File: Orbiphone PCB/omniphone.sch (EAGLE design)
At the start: 44 parts

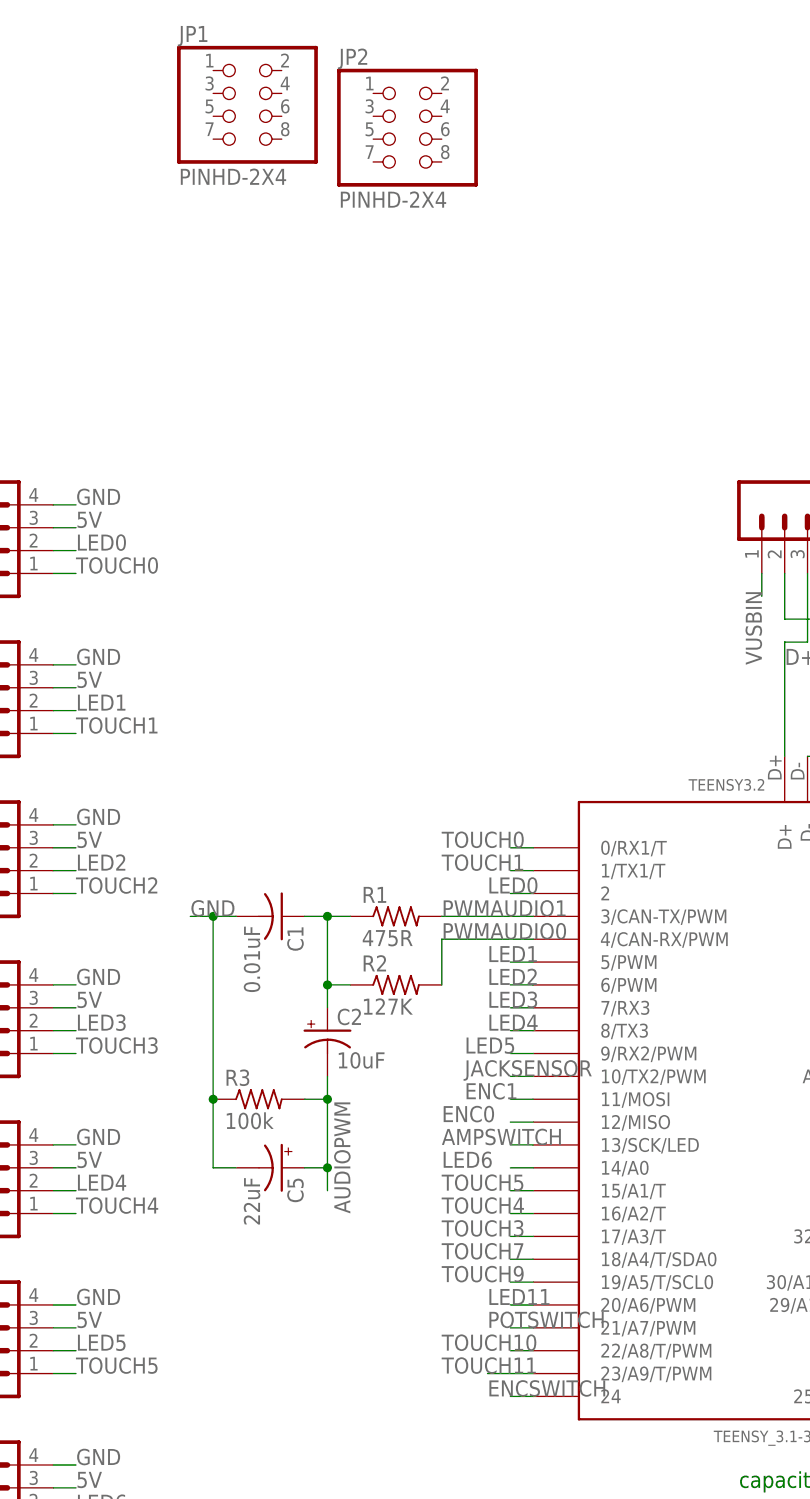
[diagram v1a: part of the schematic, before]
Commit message: changed the ampswitch as 13 doesn't work with its led on it
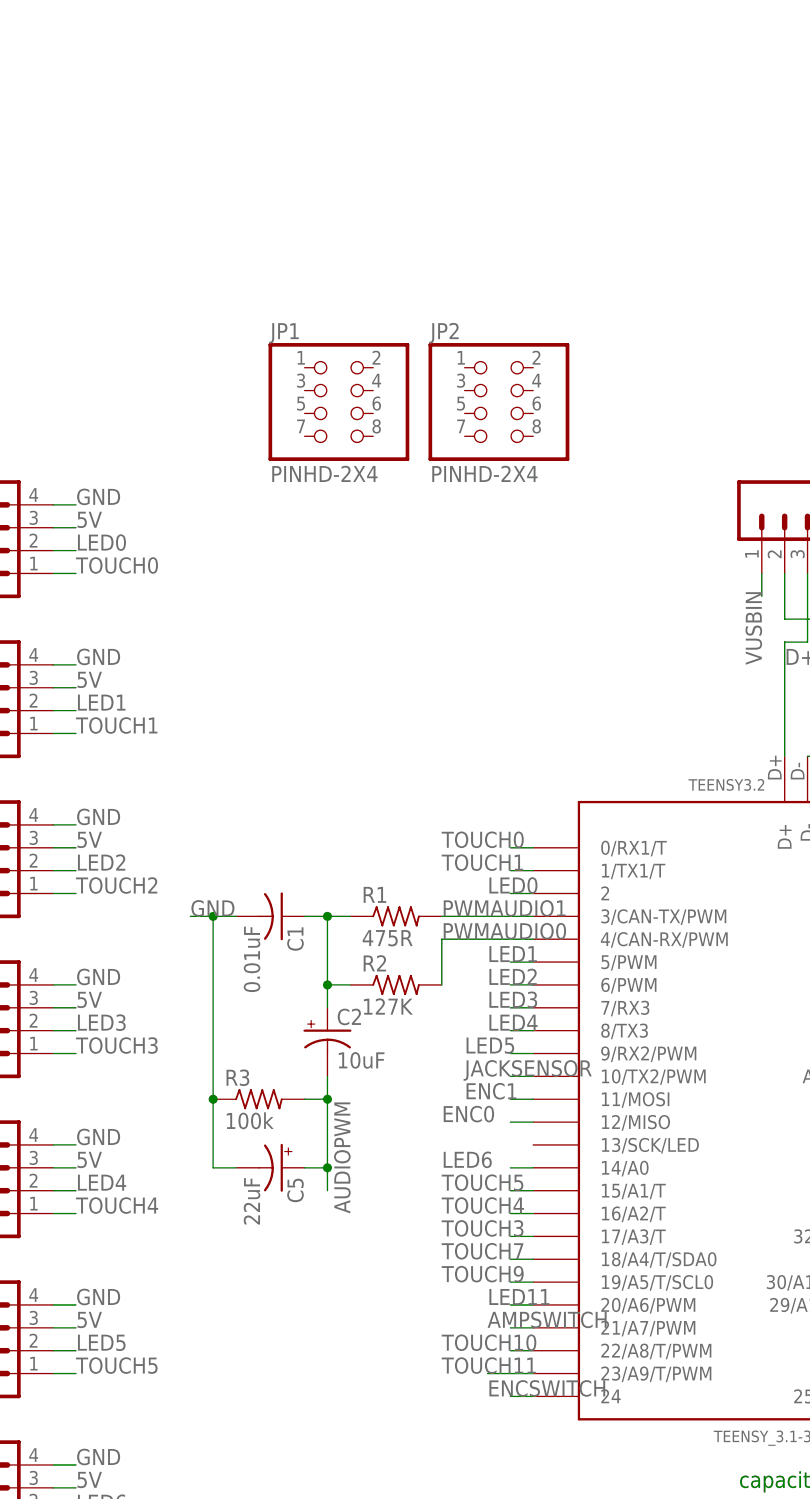
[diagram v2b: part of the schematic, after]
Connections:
- net AMPSWITCH: now also TEENSY3.2.21/A7/PWM; no longer TEENSY3.2.13/SCK/LED
- net POTSWITCH: no longer TEENSY3.2.21/A7/PWM
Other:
- moved on the sheet: JP1, JP2
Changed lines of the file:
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@@
 </instance>
 <instance part="BATTERY" gate="&gt;NAME" x="86.36" y="-5.08" smashed="yes" rot="R180"/>
-<instance part="JP1" gate="A" x="7.62" y="170.18" smashed="yes">
-<attribute name="NAME" x="1.27" y="178.435" size="1.778" layer="95"/>
-<attribute name="VALUE" x="1.27" y="162.56" size="1.778" layer="96"/>
-</instance>
-<instance part="JP2" gate="A" x="25.4" y="167.64" smashed="yes">
-<attribute name="NAME" x="19.05" y="175.895" size="1.778" layer="95"/>
-<attribute name="VALUE" x="19.05" y="160.02" size="1.778" layer="96"/>
+<instance part="JP1" gate="A" x="17.78" y="137.16" smashed="yes">
+<attribute name="NAME" x="11.43" y="145.415" size="1.778" layer="95"/>
+<attribute name="VALUE" x="11.43" y="129.54" size="1.778" layer="96"/>
+</instance>
+<instance part="JP2" gate="A" x="35.56" y="137.16" smashed="yes">
+<attribute name="NAME" x="29.21" y="145.415" size="1.778" layer="95"/>
+<attribute name="VALUE" x="29.21" y="129.54" size="1.778" layer="96"/>
 </instance>
 <instance part="R7" gate="G$1" x="91.44" y="7.62" smashed="yes">
@@
 </segment>
 <segment>
-<pinref part="TEENSY3.2" gate="G$1" pin="13/SCK/LED"/>
-<wire x1="40.64" y1="55.88" x2="38.1" y2="55.88" width="0.1524" layer="91"/>
-<label x="30.48" y="55.88" size="1.778" layer="95"/>
+<pinref part="TEENSY3.2" gate="G$1" pin="21/A7/PWM"/>
+<wire x1="40.64" y1="35.56" x2="38.1" y2="35.56" width="0.1524" layer="91"/>
+<label x="35.56" y="35.56" size="1.778" layer="95"/>
 </segment>
 </net>
@@
 <label x="104.14" y="106.68" size="1.778" layer="95"/>
 </segment>
-<segment>
-<pinref part="TEENSY3.2" gate="G$1" pin="21/A7/PWM"/>
-<wire x1="40.64" y1="35.56" x2="38.1" y2="35.56" width="0.1524" layer="91"/>
-<label x="35.56" y="35.56" size="1.778" layer="95"/>
-</segment>
-</net>
+</net>

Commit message: preparations for powerswitch modification
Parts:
- removed T/POWER: JUMPER-SMT_3_1-NC_TRACE_SILK, SparkFun-Jumpers:JUMPER-SMT_3_1-NC_TRACE_SILK
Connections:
- removed net N$4: POT.2, T/POWER.2
- removed net POTSWITCH: T/POWER.3
- net POWERENABLE: now also POT.2; no longer T/POWER.1
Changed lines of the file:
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@@
 <part name="SPEAKERDAC" library="ArvidLibrary" deviceset="SPEAKERTERMINAL" device="-3.5MM" package3d_urn="urn:adsk.eagle:package:6240635/1"/>
 <part name="SPEAKERPWM" library="ArvidLibrary" deviceset="SPEAKERTERMINAL" device="-3.5MM" package3d_urn="urn:adsk.eagle:package:6240635/1"/>
-<part name="T/POWER" library="SparkFun-Jumpers" library_urn="urn:adsk.eagle:library:528" deviceset="JUMPER-SMT_3_1-NC_TRACE" device="_SILK" package3d_urn="urn:adsk.eagle:package:39288/1"/>
 <part name="BATTERY" library="ArvidLibrary" deviceset="SPEAKERTERMINAL" device="-3.5MM" package3d_urn="urn:adsk.eagle:package:6240635/1"/>
 <part name="JP1" library="Connector" library_urn="urn:adsk.eagle:library:16378166" deviceset="PINHD-2X4" device="" package3d_urn="urn:adsk.eagle:package:22461/2"/>
@@
 <instance part="SPEAKERDAC" gate="&gt;NAME" x="96.52" y="-35.56" smashed="yes"/>
 <instance part="SPEAKERPWM" gate="&gt;NAME" x="96.52" y="-48.26" smashed="yes"/>
-<instance part="T/POWER" gate="G$1" x="111.76" y="101.6" smashed="yes" rot="R180">
-<attribute name="NAME" x="109.22" y="101.219" size="1.778" layer="95" font="vector" rot="R180"/>
-</instance>
 <instance part="BATTERY" gate="&gt;NAME" x="86.36" y="-5.08" smashed="yes" rot="R180"/>
 <instance part="JP1" gate="A" x="17.78" y="137.16" smashed="yes">
@@
 </segment>
 <segment>
-<pinref part="T/POWER" gate="G$1" pin="1"/>
-<wire x1="111.76" y1="96.52" x2="111.76" y2="93.98" width="0.1524" layer="91"/>
-<label x="104.14" y="93.98" size="1.778" layer="95"/>
+<pinref part="POT" gate="G$1" pin="2"/>
+<wire x1="137.16" y1="101.6" x2="116.84" y2="101.6" width="0.1524" layer="91"/>
+<label x="111.76" y="101.6" size="1.778" layer="95"/>
 </segment>
 </net>
@@
 <wire x1="86.36" y1="53.34" x2="88.9" y2="53.34" width="0.1524" layer="91"/>
 <label x="88.9" y="53.34" size="1.778" layer="95"/>
-</segment>
-</net>
-<net name="POTSWITCH" class="0">
-<segment>
-<pinref part="T/POWER" gate="G$1" pin="3"/>
-<wire x1="111.76" y1="106.68" x2="111.76" y2="109.22" width="0.1524" layer="91"/>
-<label x="104.14" y="106.68" size="1.778" layer="95"/>
 </segment>
 </net>
@@
 </segment>
 </net>
-<net name="N$4" class="0">
-<segment>
-<pinref part="POT" gate="G$1" pin="2"/>
-<pinref part="T/POWER" gate="G$1" pin="2"/>
-<wire x1="137.16" y1="101.6" x2="116.84" y2="101.6" width="0.1524" layer="91"/>
-</segment>
-</net>
 <net name="BATSENSOR" class="0">
 <segment>
@@
 </segment>
 </net>
+<net name="TOADD-BATCONNECTIONFORPOWERSWITCH" class="0">
+<segment>
+<wire x1="106.68" y1="106.68" x2="121.92" y2="106.68" width="0.1524" layer="91"/>
+<label x="101.6" y="106.68" size="1.778" layer="95"/>
+</segment>
+</net>
